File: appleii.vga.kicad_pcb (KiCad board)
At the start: 2 copper layers, 104.1 x 75.6 mm, 32 parts, among them J1 BUS_APPLE_II, J2 Conn_01x25, J3 Conn_01x25, J4 Conn_01x08, J5 Conn_01x03, Q1 DMG2305UX, U1 74LVC245A, U2 74LVC245A, U3 74LVC245A, U4 74LVC245A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

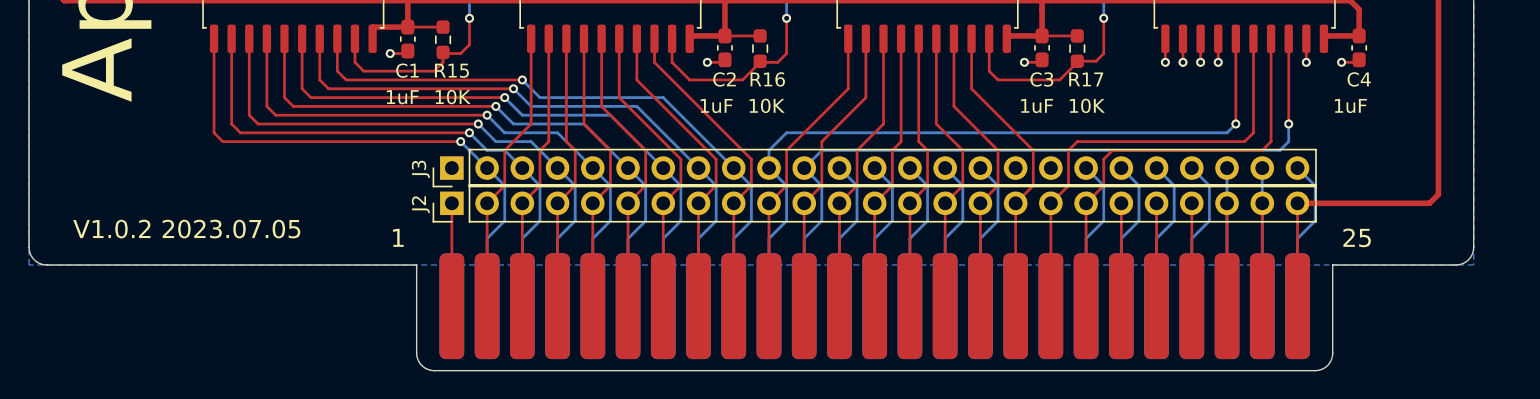
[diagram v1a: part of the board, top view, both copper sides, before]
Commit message: update board to v1.1.0
Some minor improvements based on v1.0.2 fab, assembly and test:
- correct "1uF" to "0.1uF" on decoupling caps
- reduce width of card edge connector by ~1.2mm
- increase trace widths to VCC and GND pins
- increase ground fill edge exclusion from 0 to 0.625mm
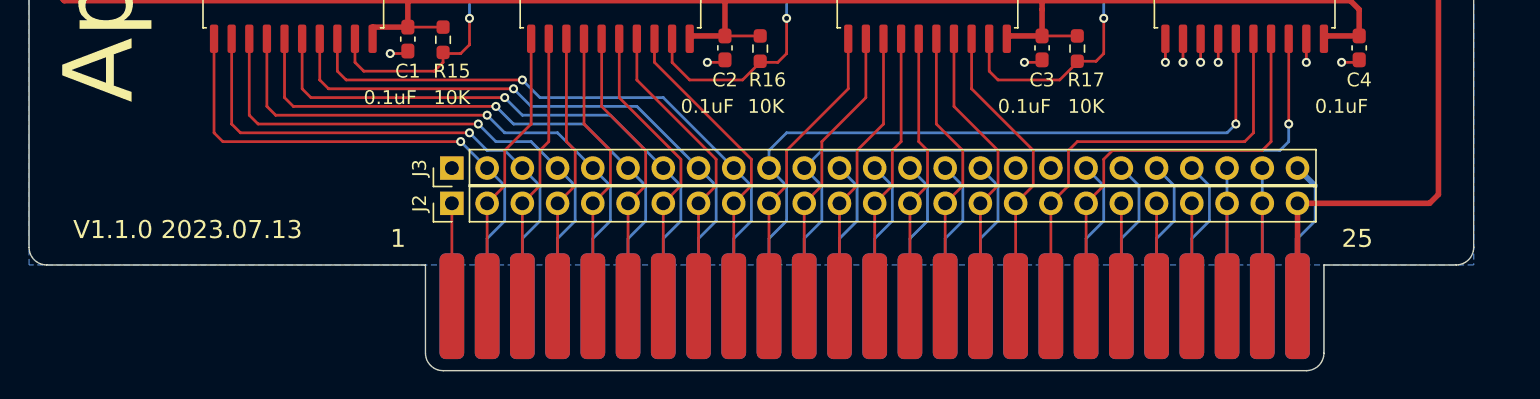
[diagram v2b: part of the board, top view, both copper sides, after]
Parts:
- C1, C2, C3, C4: value 1uF -> 0.1uF
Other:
- outline, holes or cut-outs redrawn
- board text added: "V1.1.0 2023.07.13"
- board text removed: "V1.0.2 2023.07.05"
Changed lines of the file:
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@@
         (effects (font (size 1 1) (thickness 0.15)))
     )
-    (fp_text value "1uF" (at 4.2175 0.4 180) (layer "F.SilkS")
+    (fp_text value "0.1uF" (at 4.2175 1.27 180) (layer "F.SilkS")
         (effects (font (size 1 1) (thickness 0.15)))
     )
@@
         (effects (font (size 1 1) (thickness 0.15)))
     )
-    (fp_text value "1uF" (at 4.2175 0.4 180) (layer "F.SilkS")
+    (fp_text value "0.1uF" (at 4.2175 1.27 180) (layer "F.SilkS")
         (effects (font (size 1 1) (thickness 0.15)))
     )
@@
         (effects (font (size 1 1) (thickness 0.15)))
     )
-    (fp_text value "1uF" (at 4.2175 0.635 180) (layer "F.SilkS")
+    (fp_text value "0.1uF" (at 4.2175 1.27 180) (layer "F.SilkS")
         (effects (font (size 1 1) (thickness 0.15)))
     )
@@
         (effects (font (size 1 1) (thickness 0.15)))
     )
-    (fp_text value "1uF" (at 4.2175 0.635 180) (layer "F.SilkS")
+    (fp_text value "0.1uF" (at 4.2175 1.27 180) (layer "F.SilkS")
         (effects (font (size 1 1) (thickness 0.15)))
     )
@@
     )
   )
-  (gr_arc (start 160.02 140.335) (mid 159.648026 141.233026) (end 158.75 141.605)
+  (gr_arc (start 159.385 140.335) (mid 159.013026 141.233026) (end 158.115 141.605)
     (stroke (width 0.1) (type solid)) (layer "Edge.Cuts"))
-  (gr_line (start 93.98 133.985) (end 93.98 140.335)
+  (gr_line (start 94.615 133.985) (end 94.615 140.335)
     (stroke (width 0.1) (type solid)) (layer "Edge.Cuts"))
   (gr_line (start 170.18 132.715) (end 170.18 67.31)
     (stroke (width 0.1) (type solid)) (layer "Edge.Cuts"))
-  (gr_line (start 160.02 133.985) (end 168.91 133.985)
+  (gr_line (start 159.385 133.985) (end 168.91 133.985)
     (stroke (width 0.1) (type solid)) (layer "Edge.Cuts"))
   (gr_arc (start 170.18 132.715) (mid 169.808026 133.613026) (end 168.91 133.985)
@@
   (gr_arc (start 66.04 67.31) (mid 66.411974 66.411974) (end 67.31 66.04)
     (stroke (width 0.1) (type solid)) (layer "Edge.Cuts"))
-  (gr_line (start 95.25 141.605) (end 158.75 141.605)
+  (gr_line (start 95.885 141.605) (end 158.115 141.605)
     (stroke (width 0.1) (type solid)) (layer "Edge.Cuts"))
-  (gr_line (start 160.02 140.335) (end 160.02 133.985)
+  (gr_line (start 159.385 140.335) (end 159.385 133.985)
     (stroke (width 0.1) (type solid)) (layer "Edge.Cuts"))
   (gr_arc (start 168.91 66.04) (mid 169.808026 66.411974) (end 170.18 67.31)
@@
   (gr_line (start 66.04 67.31) (end 66.04 132.715)
     (stroke (width 0.1) (type solid)) (layer "Edge.Cuts"))
-  (gr_line (start 67.31 133.985) (end 93.98 133.985)
+  (gr_line (start 67.31 133.985) (end 94.615 133.985)
     (stroke (width 0.1) (type solid)) (layer "Edge.Cuts"))
   (gr_line (start 168.91 66.04) (end 67.31 66.04)
     (stroke (width 0.1) (type solid)) (layer "Edge.Cuts"))
-  (gr_arc (start 95.25 141.605) (mid 94.351974 141.233026) (end 93.98 140.335)
+  (gr_arc (start 95.885 141.605) (mid 94.986974 141.233026) (end 94.615 140.335)
     (stroke (width 0.1) (type solid)) (layer "Edge.Cuts"))
   (gr_arc (start 67.31 133.985) (mid 66.411974 133.613026) (end 66.04 132.715)
@@
     (effects (font (size 1.3 1.3) (thickness 0.25)) (justify left))
   )
-  (gr_text "V1.0.2 2023.07.05" (at 69.215 131.445) (layer "F.SilkS")
+  (gr_text "V1.1.0 2023.07.13" (at 69.215 131.445) (layer "F.SilkS")
     (effects (font (size 1.3 1.3) (thickness 0.25)) (justify left))
   )
@@
   (via (at 114.935 119.38) (size 0.65) (drill 0.35) (layers "F.Cu" "B.Cu") (net 1))
   (via (at 160.655 119.38) (size 0.65) (drill 0.35) (layers "F.Cu" "B.Cu") (net 1))
-  (segment (start 157.48 127) (end 158.75 128.27) (width 0.2) (layer "B.Cu") (net 1))
+  (segment (start 157.48 127) (end 158.75 128.27) (width 0.4) (layer "B.Cu") (net 1))
   (segment (start 158.75 128.27) (end 158.75 130.81) (width 0.2) (layer "B.Cu") (net 1))
   (segment (start 158.75 130.81) (end 157.48 132.08) (width 0.2) (layer "B.Cu") (net 1))
-  (segment (start 157.48 132.08) (end 157.48 137.16) (width 0.2) (layer "B.Cu") (net 1))
+  (segment (start 157.48 132.08) (end 157.48 137.16) (width 0.4) (layer "B.Cu") (net 1))
   (segment (start 130.175 90.17) (end 131.445 91.44) (width 0.2) (layer "F.Cu") (net 7))
   (segment (start 131.445 91.44) (end 148.3125 91.44) (width 0.2) (layer "F.Cu") (net 7))
@@
   (segment (start 151.13 128.27) (end 151.13 130.81) (width 0.2) (layer "B.Cu") (net 46))
   (segment (start 149.86 132.08) (end 149.86 137.16) (width 0.2) (layer "B.Cu") (net 46))
-  (segment (start 157.48 137.16) (end 157.48 129.54) (width 0.2) (layer "F.Cu") (net 47))
+  (segment (start 157.48 137.16) (end 157.48 129.54) (width 0.4) (layer "F.Cu") (net 47))
   (segment (start 70.485 75.565) (end 71.12 74.93) (width 0.4) (layer "F.Cu") (net 47))
   (segment (start 71.12 74.93) (end 75.2325 74.93) (width 0.4) (layer "F.Cu") (net 47))
